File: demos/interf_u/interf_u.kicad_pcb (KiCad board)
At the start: 2 copper layers, 115.6 x 108 mm, 25 parts, among them P1 DB25FEMELLE, U1 74LS245, U2 74LS688, U3 74LS541, U5 628128, U8 EP600, U9 4003APG120, X1 8MHz

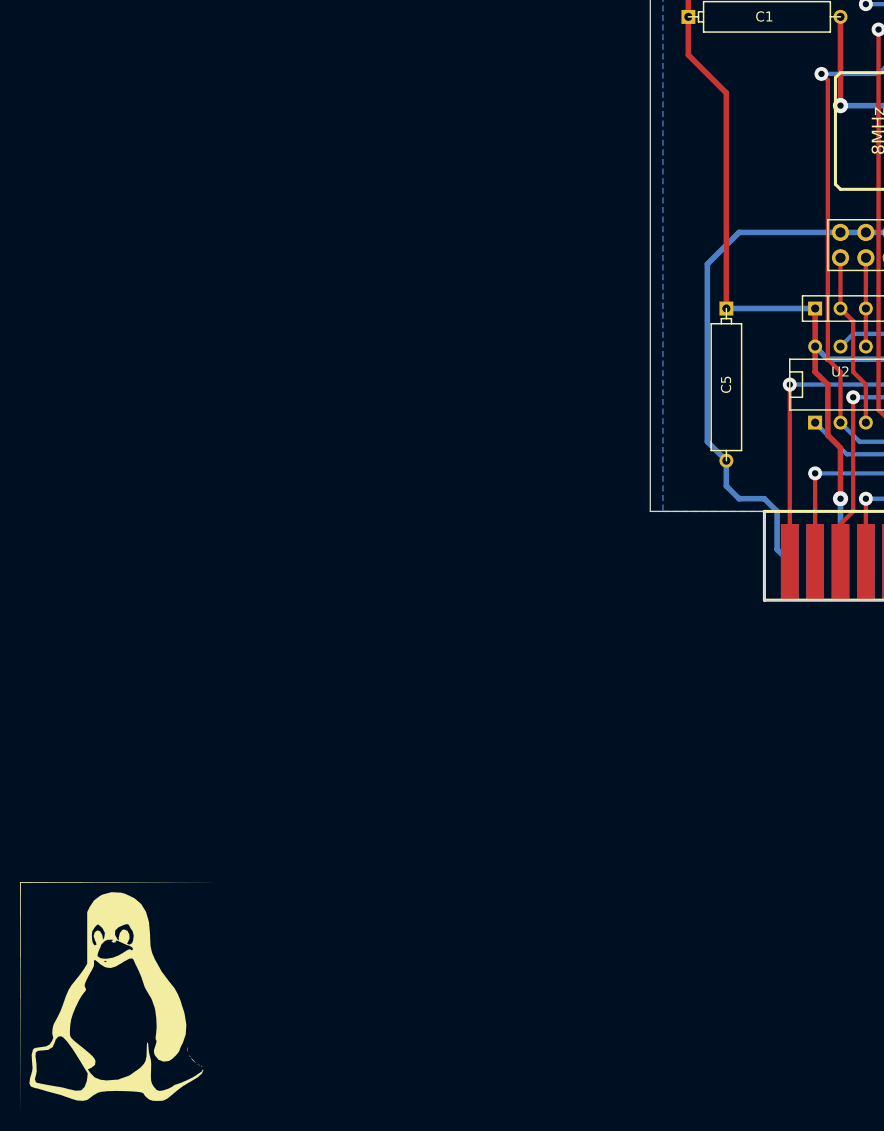
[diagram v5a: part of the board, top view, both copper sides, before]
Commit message: Update clipper library version (from 6.21) to the latest (currently  6.4.0 ,  2 July 2015) which fixes some bugs.
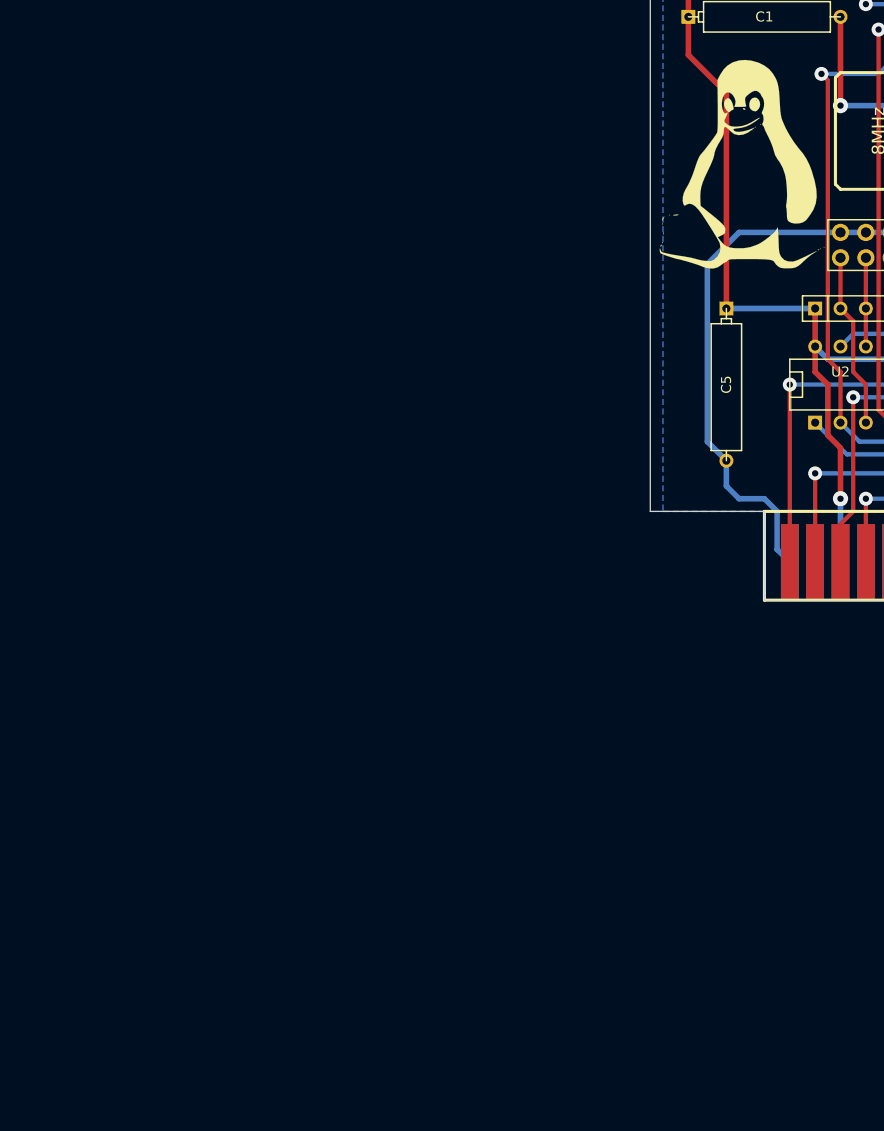
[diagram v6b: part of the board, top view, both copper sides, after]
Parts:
- removed G1: LOGO, 
- added G***: LOGO, LOGO, F.Cu at (89.0, 98.6)

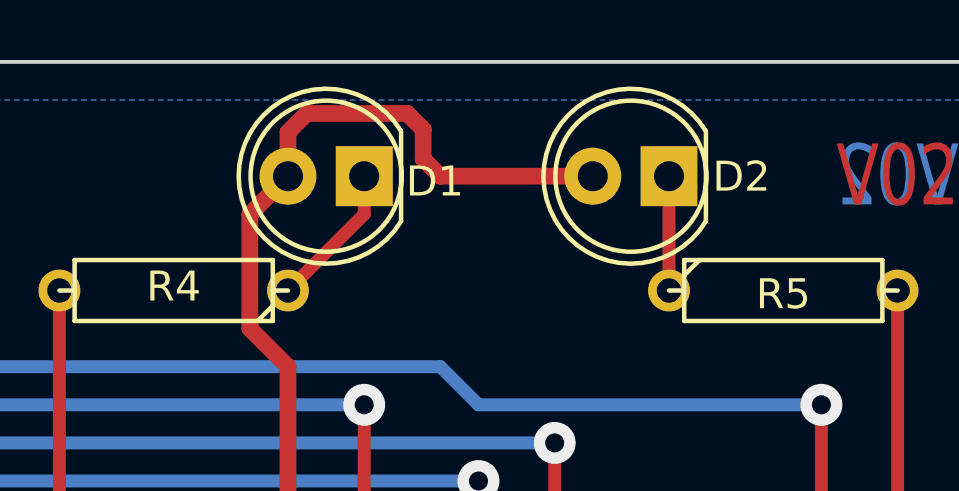
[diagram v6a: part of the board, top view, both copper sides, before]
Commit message: Pcbnew and Gerbview: layer manager: use double click to edit color (as usual to edit someting) and simple click (as previously) to select the layer. Reason: avoid opening the color dialog each time a new layer is selected. Update interf_u demo to use recent library components..
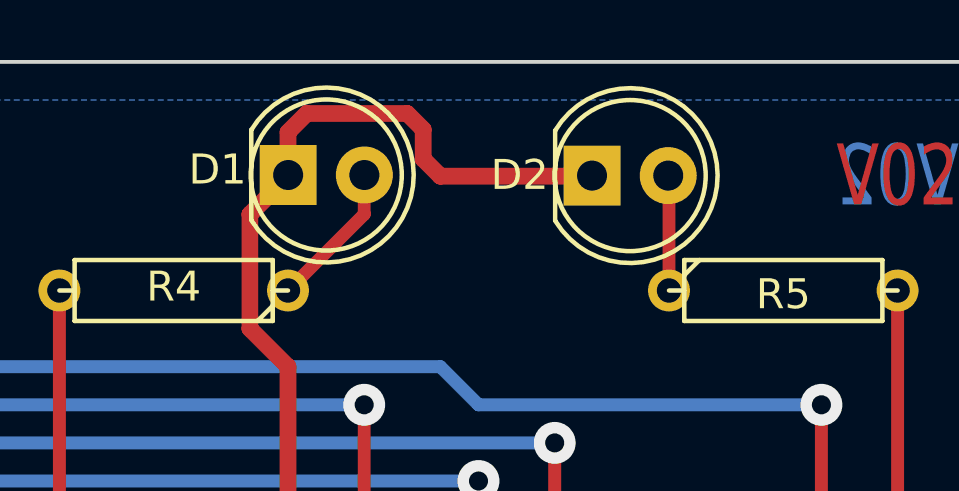
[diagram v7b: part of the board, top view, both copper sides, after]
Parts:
- moved D2 2.57 mm to (165.7, 38.1), turned to 0 degrees
- moved D1 2.54 mm to (155.6, 38.1), turned to 0 degrees
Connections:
- BUS1 pad 10: (no net) -> Net-(BUS1-Pad10)
- BUS1 pad 11: (no net) -> Net-(BUS1-Pad11)
- BUS1 pad 12: (no net) -> Net-(BUS1-Pad12)
- BUS1 pad 15: (no net) -> Net-(BUS1-Pad15)
- BUS1 pad 16: (no net) -> Net-(BUS1-Pad16)
- BUS1 pad 17: (no net) -> Net-(BUS1-Pad17)
- BUS1 pad 18: (no net) -> Net-(BUS1-Pad18)
- BUS1 pad 19: (no net) -> Net-(BUS1-Pad19)
- BUS1 pad 20: (no net) -> Net-(BUS1-Pad20)
- BUS1 pad 21: (no net) -> Net-(BUS1-Pad21)
- BUS1 pad 22: (no net) -> Net-(BUS1-Pad22)
- BUS1 pad 23: (no net) -> Net-(BUS1-Pad23)
- BUS1 pad 24: (no net) -> Net-(BUS1-Pad24)
- BUS1 pad 25: (no net) -> Net-(BUS1-Pad25)
- BUS1 pad 26: (no net) -> Net-(BUS1-Pad26)
- BUS1 pad 27: (no net) -> Net-(BUS1-Pad27)
- BUS1 pad 28: (no net) -> Net-(BUS1-Pad28)
- BUS1 pad 30: (no net) -> Net-(BUS1-Pad30)
- BUS1 pad 32: (no net) -> Net-(BUS1-Pad32)
- BUS1 pad 4: (no net) -> Net-(BUS1-Pad4)
- BUS1 pad 41: (no net) -> Net-(BUS1-Pad41)
- BUS1 pad 43: (no net) -> Net-(BUS1-Pad43)
- BUS1 pad 44: (no net) -> Net-(BUS1-Pad44)
- BUS1 pad 45: (no net) -> Net-(BUS1-Pad45)
- BUS1 pad 46: (no net) -> Net-(BUS1-Pad46)
- BUS1 pad 47: (no net) -> Net-(BUS1-Pad47)
- BUS1 pad 48: (no net) -> Net-(BUS1-Pad48)
- BUS1 pad 49: (no net) -> Net-(BUS1-Pad49)
- BUS1 pad 5: (no net) -> Net-(BUS1-Pad5)
- BUS1 pad 50: (no net) -> Net-(BUS1-Pad50)
- BUS1 pad 6: (no net) -> Net-(BUS1-Pad6)
- BUS1 pad 7: (no net) -> Net-(BUS1-Pad7)
- BUS1 pad 8: (no net) -> Net-(BUS1-Pad8)
- BUS1 pad 9: (no net) -> Net-(BUS1-Pad9)
- D1 pad 1: Net-(D1-Pad1) -> GND
- D1 pad 2: GND -> Net-(D1-Pad2)
- D2 pad 1: Net-(D2-Pad1) -> GND
- D2 pad 2: GND -> Net-(D2-Pad2)
- R4 pad 1: Net-(D1-Pad1) -> Net-(D1-Pad2)
- R5 pad 1: Net-(D2-Pad1) -> Net-(D2-Pad2)
- RR1 pad 10: (no net) -> Net-(RR1-Pad10)
- U3 pad 11: (no net) -> Net-(U3-Pad11)
- U8 pad 10: (no net) -> Net-(U8-Pad10)
- U8 pad 8: (no net) -> Net-(U8-Pad8)
- U8 pad 9: (no net) -> Net-(U8-Pad9)
- U9 pad A1: (no net) -> Net-(U9-PadA1)
- U9 pad A2: (no net) -> Net-(U9-PadA2)
- U9 pad A3: (no net) -> Net-(U9-PadA3)
- U9 pad B1: (no net) -> Net-(U9-PadB1)
- U9 pad B10: (no net) -> Net-(U9-PadB10)
- U9 pad B13: (no net) -> Net-(U9-PadB13)
- U9 pad B4: (no net) -> Net-(U9-PadB4)
- U9 pad B5: (no net) -> Net-(U9-PadB5)
- U9 pad C5: (no net) -> Net-(U9-PadC5)
- U9 pad E11: (no net) -> Net-(U9-PadE11)
- U9 pad E2: (no net) -> Net-(U9-PadE2)
- U9 pad E3: (no net) -> Net-(U9-PadE3)
- U9 pad J11: (no net) -> Net-(U9-PadJ11)
- U9 pad J3: (no net) -> Net-(U9-PadJ3)
- U9 pad K12: (no net) -> Net-(U9-PadK12)
- U9 pad L5: (no net) -> Net-(U9-PadL5)
- U9 pad L6: (no net) -> Net-(U9-PadL6)
- U9 pad L9: (no net) -> Net-(U9-PadL9)
- U9 pad M1: (no net) -> Net-(U9-PadM1)
- U9 pad M2: (no net) -> Net-(U9-PadM2)
- U9 pad N1: (no net) -> Net-(U9-PadN1)
- U9 pad N12: (no net) -> Net-(U9-PadN12)
- U9 pad N3: (no net) -> Net-(U9-PadN3)
- U9 pad N5: (no net) -> Net-(U9-PadN5)
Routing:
- net Net-(D1-Pad2): track 0.00 -> 4.86 mm
- net Net-(D1-Pad1): track 4.86 -> 0.00 mm
- net Net-(D2-Pad2): track 0.00 -> 3.81 mm
- net Net-(D2-Pad1): track 3.81 -> 0.00 mm
